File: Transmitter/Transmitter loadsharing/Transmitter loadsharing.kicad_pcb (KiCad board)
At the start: 4 copper layers, 145 x 50.8 mm, 115 parts, among them J1 Conn_Coaxial, J10 Conn_01x01, J11 Conn_01x01, J12 Conn_01x01, J13 Conn_01x01, J14 Conn_01x01, J15 Conn_01x01, J16 Conn_01x01, J17 Conn_Coaxial, J18 Conn_Coaxial, J19 Conn_Coaxial, J2 Conn_01x03, J20 Conn_01x01, J21 Conn_01x01, J22 Conn_01x01, J23 Conn_01x01, J24 Conn_01x01, J25 Conn_01x01, J3 Conn_01x03, J4 Conn_01x02_Socket, J5 Conn_01x02, J6 Conn_01x01, J7 Conn_01x02, J8 Conn_01x02_Socket, J9 Conn_01x01, U1 OPA3692IDBQR, U10 LT3094EMSE-PBF, U11 LT3094EMSE-PBF, U2 THS3091D, U3 THS3091D, U4 THS3091D, U5 THS3091D, U6 THS3091D, U7 THS3091D, U8 LT3045EMSE-PBF, U9 LT3045EMSE-PBF

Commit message: version before review with Saul
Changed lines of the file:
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@@
 			)
 		)
-		(property ki_fp_filters "*BNC* *SMA* *SMB* *SMC* *Cinch* *LEMO* *UMRF* *MCX* *U.FL*")
-		(sheetname "Root")
-		(sheetfile "Transmitter loadsharing.kicad_sch")
 		(attr through_hole)
 		(fp_line
@@
 		)
 		(model "${KICAD8_3DMODEL_DIR}/Connector_Coaxial.3dshapes/BNC_Amphenol_B6252HB-NPP3G-50_Horizontal.wrl"
+			(hide yes)
 			(offset
 				(xyz 0 0 0)
@@
 			)
 		)
+		(model "C:/Projects/KiCad/Spiral/Kicad Degree project GIT/Degree-Project-KiCad/B6252HB-NPP3G-50/3D/B6252HB-NPP3G-50.stp"
+			(offset
+				(xyz 0 -1 8)
+			)
+			(scale
+				(xyz 1 1 1)
+			)
+			(rotate
+				(xyz -90 0 180)
+			)
+		)
 	)
 	(footprint "Opa3692 SOIC:DBQ16"
@@
 			)
 		)
-		(property ki_fp_filters "*BNC* *SMA* *SMB* *SMC* *Cinch* *LEMO* *UMRF* *MCX* *U.FL*")
-		(sheetname "Root")
-		(sheetfile "Transmitter loadsharing.kicad_sch")
 		(attr through_hole)
 		(fp_line
@@
 		)
 		(model "${KICAD8_3DMODEL_DIR}/Connector_Coaxial.3dshapes/BNC_Amphenol_B6252HB-NPP3G-50_Horizontal.wrl"
+			(hide yes)
 			(offset
 				(xyz 0 0 0)
@@
 			)
 		)
+		(model "C:/Projects/KiCad/Spiral/Kicad Degree project GIT/Degree-Project-KiCad/B6252HB-NPP3G-50/3D/B6252HB-NPP3G-50.stp"
+			(offset
+				(xyz 0 -1 8)
+			)
+			(scale
+				(xyz 1 1 1)
+			)
+			(rotate
+				(xyz -90 0 180)
+			)
+		)
 	)
 	(footprint "Capacitor_SMD:C_0603_1608Metric_Pad1.08x0.95mm_HandSolder"
@@
 		(tags "resistor handsolder")
 		(property "Reference" "R26"
-			(at 0 -1.43 90)
-			(layer "B.SilkS")
+			(at 0 -1.43 -90)
+			(layer "F.SilkS")
 			(effects
 				(font
@@
 					(thickness 0.15)
 				)
-				(justify mirror)
 			)
 		)

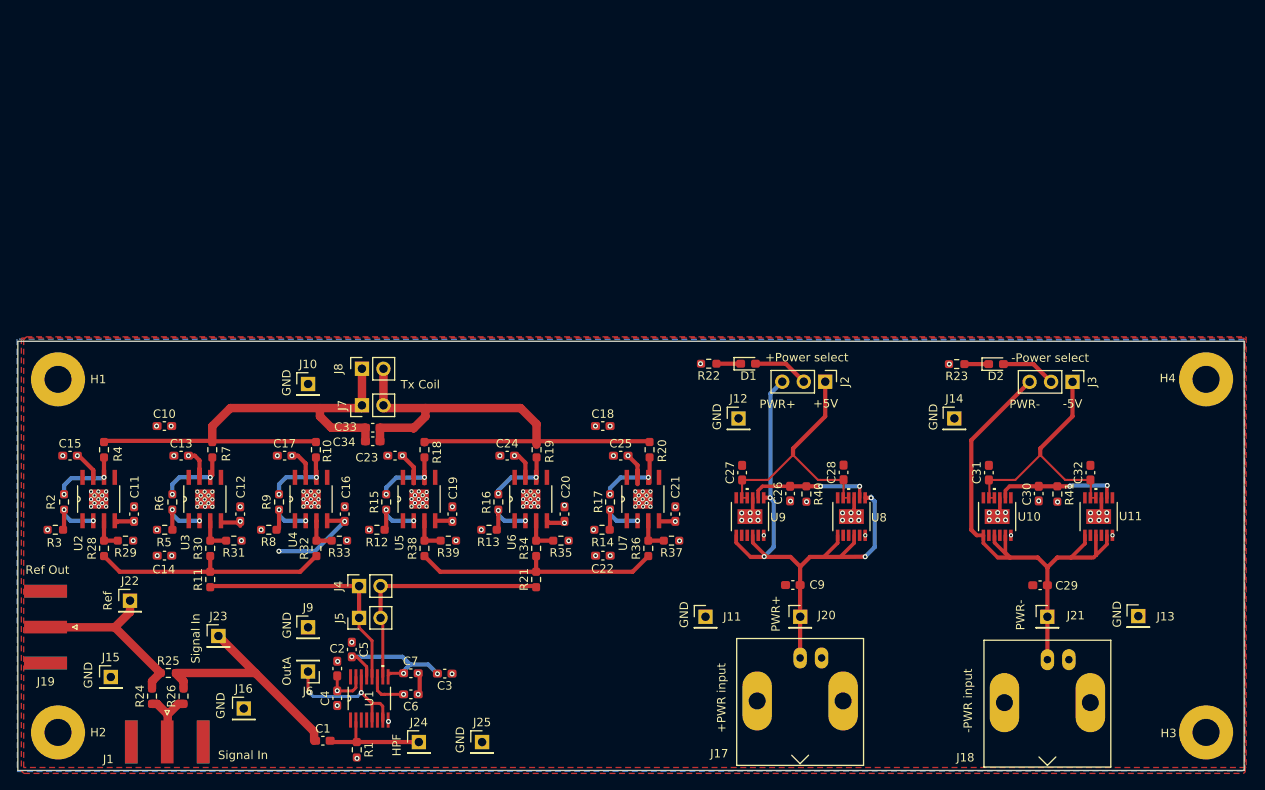
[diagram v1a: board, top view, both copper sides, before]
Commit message: Added via stiching to TX board, moved almost all vias off of pads, increased the trace width for the power supply and changed coil connector to horizontal socket
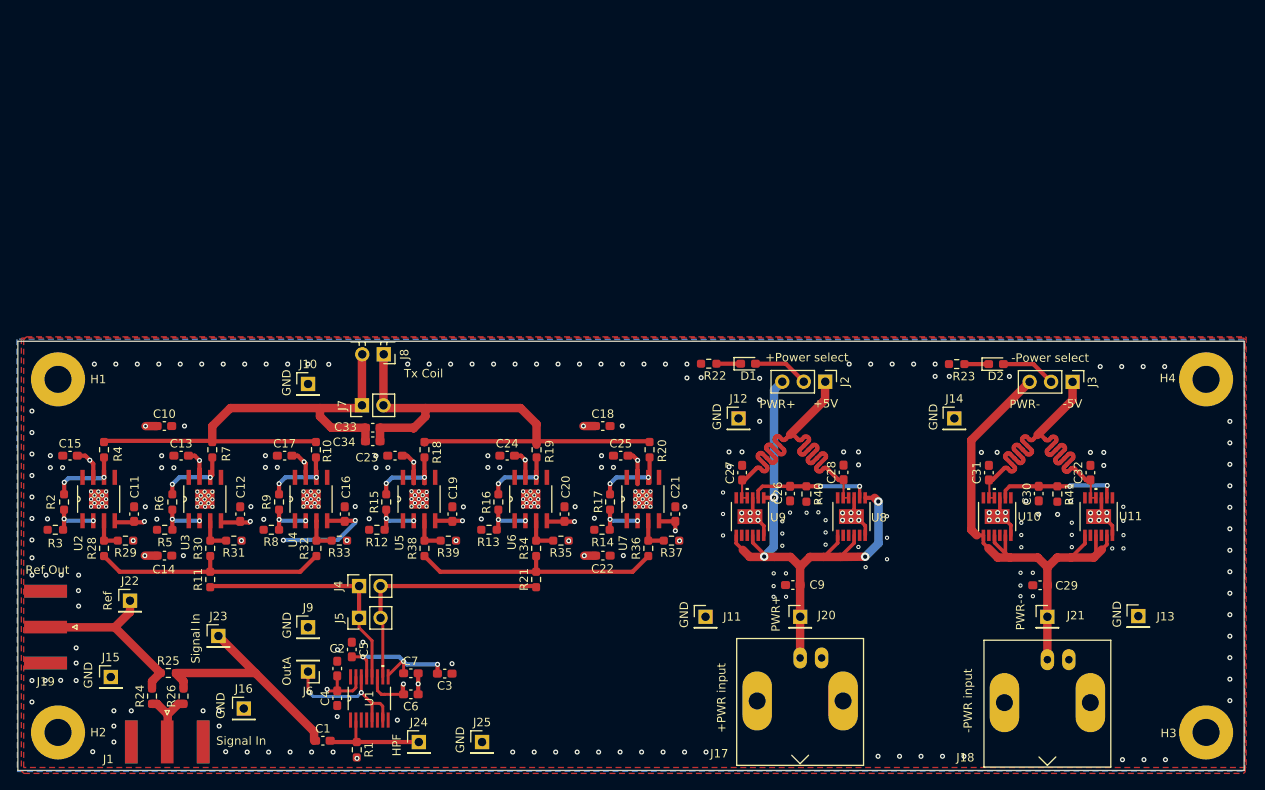
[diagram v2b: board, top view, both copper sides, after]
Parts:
- C11, C12, C13, C15, C16, C17, C19, C20, C21, C23, C24, C25: value 0.1 nF -> 0.1 uF
- J8: footprint Connector_PinSocket_2.54mm:PinSocket_1x02_P2.54mm_Vertical -> Connector_PinSocket_2.54mm:PinSocket_1x02_P2.54mm_Horizontal
- moved J8 3.09 mm to (129.8, 89.4), turned to -90 degrees
- moved R8 0.30 mm to (116.5, 110.1)
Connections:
- J8 pad 1: /coil load start -> /coil load end
- J8 pad 2: /coil load end -> /coil load start
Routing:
- net /-5V_In: track 30.2 -> 50.0 mm
- net /+5V_In: track 30.2 -> 50.0 mm
- net -5V: track 48.0 -> 57.1 mm
- net GND: track 10.1 -> 18.5 mm, vias 148 -> 313
- net +5V: track 42.7 -> 50.8 mm
- net /coil load end: track 61.9 -> 63.7 mm
- net /coil load start: track 58.6 -> 60.1 mm
- net Net-(U4-VIN-): track 6.53 -> 5.64 mm
- net Net-(U2-VIN-): track 6.79 -> 5.91 mm
- net Net-(U3-VIN-): track 6.10 -> 5.31 mm
- net /PWR+: track 69.3 -> 70.0 mm
- net Net-(U6-VIN-): track 6.33 -> 5.70 mm
- net Net-(U6-VOUT): track 8.49 -> 9.05 mm

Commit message: Fixed spacing between ICs, tried to make traces the same length each of the loadsharing op-amps
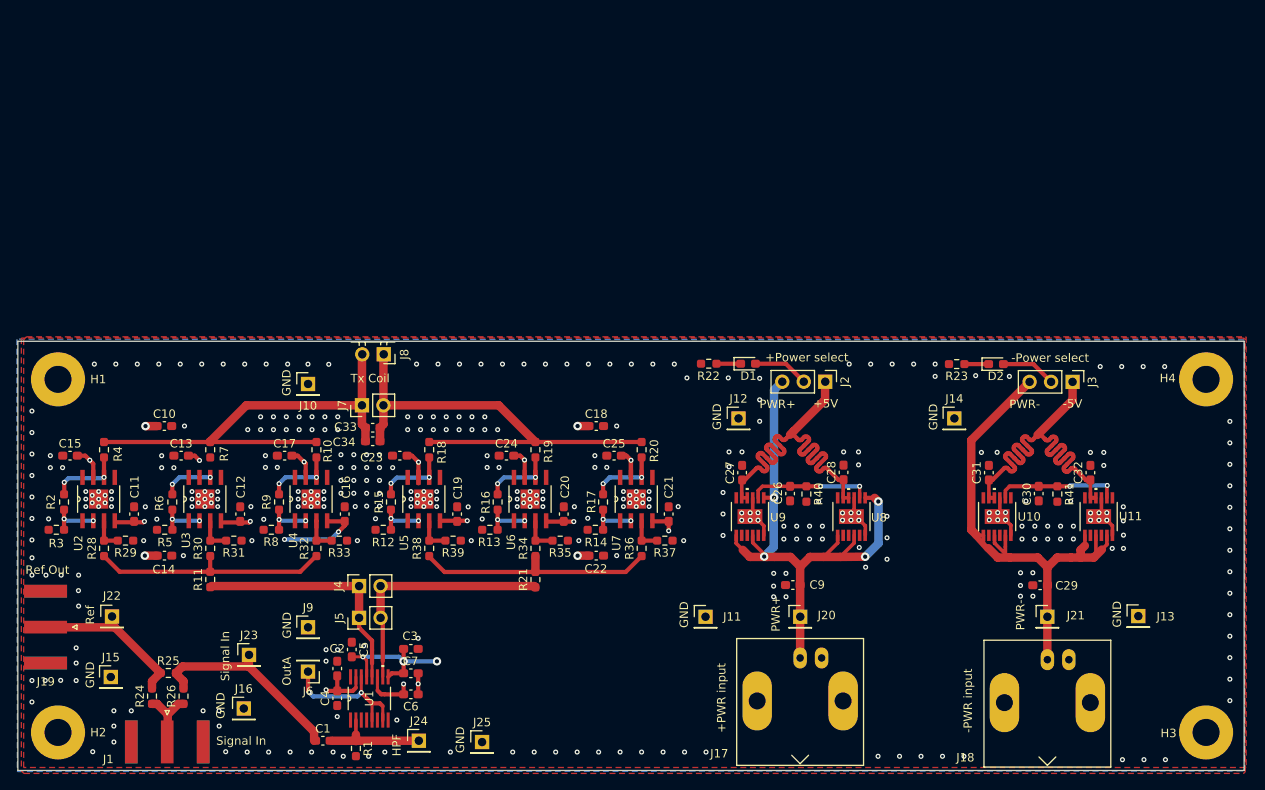
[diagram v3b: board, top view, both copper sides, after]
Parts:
- moved C3 4.96 mm to (133.0, 124.2)
- moved J23 4.25 mm to (113.8, 124.9)
- moved J22 2.83 mm to (97.6, 120.4)
- moved R20 0.94 mm to (160.2, 100.6)
- moved R17 0.82 mm to (155.7, 106.8)
- moved C21 0.79 mm to (163.4, 108.3)
- moved C22 0.79 mm to (154.9, 113.2)
- moved C25 0.79 mm to (157.0, 101.4)
- moved R14 0.79 mm to (154.8, 110.1)
- moved R36 0.79 mm to (160.2, 112.3)
- moved R37 0.79 mm to (163.0, 111.4)
- moved U7 0.79 mm to (159.6, 106.5)
- moved C18 0.77 mm to (154.9, 97.8)
- moved R12 0.75 mm to (129.7, 110.1)
- moved C19 0.56 mm to (138.4, 108.3)
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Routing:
- net /coil load end: track 63.7 -> 55.6 mm
- net +5V: track 50.8 -> 44.8 mm
- net /coil load start: track 60.1 -> 55.4 mm
- net Net-(J23-Pin_1): track 28.7 -> 24.5 mm
- net -5V: track 57.1 -> 54.1 mm
- net /Ref out: track 21.8 -> 19.4 mm
- net Net-(U3-VOUT): track 8.40 -> 6.02 mm
- net /PWR-: track 63.1 -> 64.9 mm
- net /loadshare input -: track 29.9 -> 28.6 mm
- net GND: vias 313 -> 364

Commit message: git being weird
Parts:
- C10, C14, C18, C2, C22, C3: value 6.8 uF -> 6.8uF
- C11, C12, C13, C15, C16, C17, C19, C20, C21, C23, C24, C25, C4: value 0.1 uF -> 0.1uF
- C26, C30: value 0.47u -> 0.47uF
- C27, C28, C31, C32, C9: value 10u -> 10uF
- C29: value 22u -> 22uF
- R1, R24, R25, R26: value 50 Ohm -> 50Ω
- R10, R18, R19, R20, R4, R7: value R -> Ro
- R11, R21: value 1 Ohm -> 1Ω
- R12, R13, R14, R3, R5, R8: value 250 Ohm -> Rg
- R15, R16, R17, R2, R6, R9: value 1 kOhm -> Rf
- R22, R23: value R -> Rled
- R29, R31, R33, R35, R37, R39: value R -> Rt
- R30, R32, R34, R36, R38: value 0 Ohm -> 0Ω
- moved R41 37.8 mm to (209.6, 68.1)
- moved C1 37.8 mm to (122.8, 97.2)
- moved C11 37.8 mm to (100.5, 70.4)
- moved C12 37.8 mm to (113.0, 70.4)
- moved C16 37.8 mm to (125.4, 70.4)
- moved C19 37.8 mm to (138.7, 70.4)
- moved C2 37.8 mm to (124.5, 88.7)
- moved C20 37.8 mm to (151.3, 70.4)
- moved C21 37.8 mm to (163.7, 70.4)
- moved C26 37.8 mm to (178.1, 68.0)
- moved C30 37.8 mm to (207.5, 68.0)
- moved C5 37.8 mm to (126.2, 86.4)
- moved C7 37.8 mm to (133.2, 89.3)
- moved C9 37.8 mm to (178.4, 78.8)
- moved H2 37.8 mm to (91.5, 96.2)
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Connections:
- U10 pad 12: unconnected-(U10-OUT-Pad12) -> /-5V_In
- U10 pad 13: GND -> /PWR-
- U10 pad 2: unconnected-(U10-IN-Pad2) -> /PWR-
- U11 pad 12: unconnected-(U11-OUT-Pad12) -> /-5V_In
- U11 pad 13: GND -> /PWR-
- U11 pad 2: unconnected-(U11-IN-Pad2) -> /PWR-
- U8 pad 12: unconnected-(U8-OUT-Pad12) -> /+5V_In
- U8 pad 2: unconnected-(U8-IN-Pad2) -> /PWR+
- U8 pad 3: unconnected-(U8-IN-Pad3) -> /PWR+
- U9 pad 12: unconnected-(U9-OUT-Pad12) -> /+5V_In
- U9 pad 2: unconnected-(U9-IN-Pad2) -> /PWR+
- U9 pad 3: unconnected-(U9-IN-Pad3) -> /PWR+
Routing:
- net /+5V_In: track 50.0 -> 57.8 mm
- net /PWR+: track 70.0 -> 63.6 mm
- net /-5V_In: track 49.7 -> 55.7 mm
- net Net-(U3-VOUT): track 6.02 -> 8.37 mm
- net +5V: track 44.8 -> 46.8 mm
- net GND: track 18.5 -> 16.6 mm, vias 364 -> 299
- net /PWR-: track 64.9 -> 64.3 mm
- added copper zone on F.Cu, net /PWR+
- added copper zone on F.Cu, net /PWR-

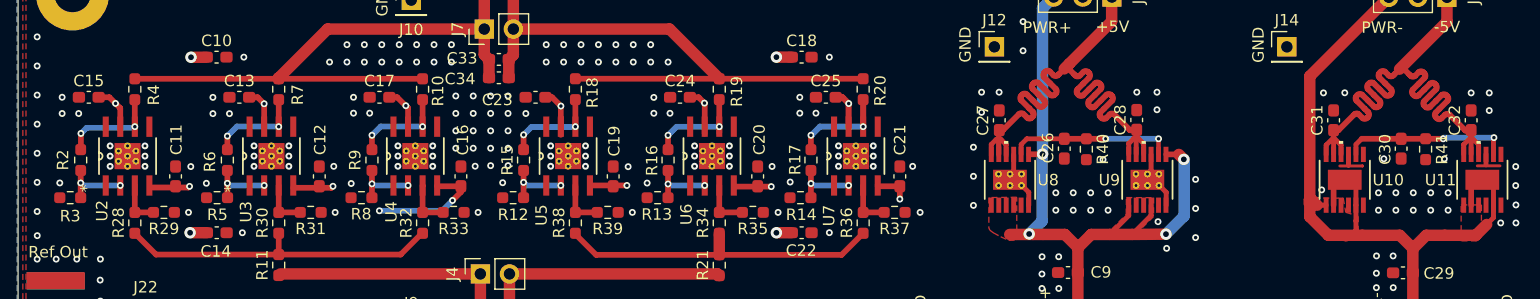
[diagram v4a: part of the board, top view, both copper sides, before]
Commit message: Changed symbol for THS to add EPAD connection, fixed thermal vias on footprint, fixed THS3091 dir
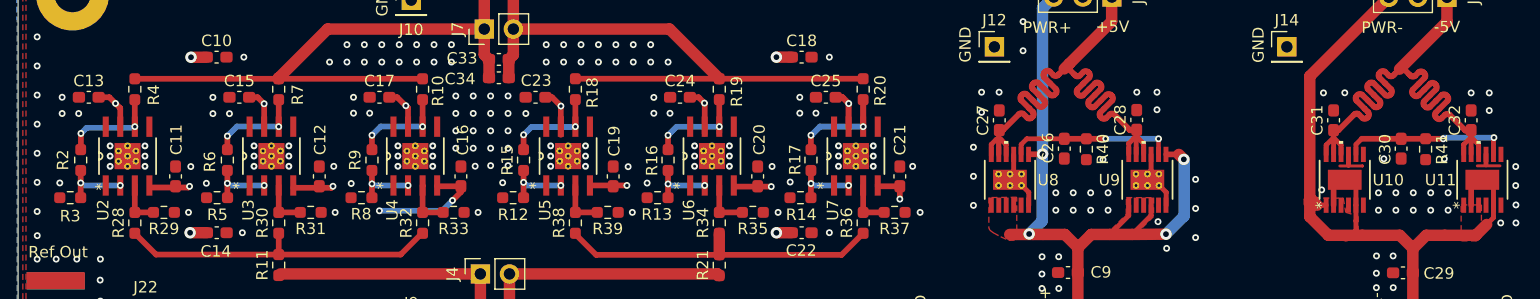
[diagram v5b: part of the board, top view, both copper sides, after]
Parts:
- U3, U4, U5, U6, U7: footprint THS3091DDR:DDA8_2P28X2P28 -> THS3091:DDA8_2P28X2P28
- renumbered C15 to C13, C13 to C15
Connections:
- C27 pad 1: /+5V_In -> +5V
- C28 pad 1: /+5V_In -> +5V
- C31 pad 1: /-5V_In -> -5V
- C32 pad 1: /-5V_In -> -5V
- J2 pad 1: /+5V_In -> +5V
- J3 pad 1: /-5V_In -> -5V
- U10 pad 10: /-5V_In -> -5V
- U10 pad 11: /-5V_In -> -5V
- U10 pad 12: /-5V_In -> -5V
- U11 pad 10: /-5V_In -> -5V
- U11 pad 11: /-5V_In -> -5V
- U11 pad 12: /-5V_In -> -5V
- U8 pad 10: /+5V_In -> +5V
- U8 pad 11: /+5V_In -> +5V
- U8 pad 12: /+5V_In -> +5V
- U9 pad 10: /+5V_In -> +5V
- U9 pad 11: /+5V_In -> +5V
- U9 pad 12: /+5V_In -> +5V
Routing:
- net +5V: track 46.8 -> 104.6 mm
- net /+5V_In: track 57.8 -> 0.00 mm
- net -5V: track 54.1 -> 109.8 mm
- net /-5V_In: track 55.7 -> 0.00 mm

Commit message: Drew a footprint for a BNC edge connector 112640, made sure coils are centered and as symmetrical as possible:wq
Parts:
- J8: value Conn_01x02_Socket -> Conn_01x02_Socket Horizontal
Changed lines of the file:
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@@
 			)
 		)
-		(property "Footprint" "DDA8_2P28X2P28"
+		(property "Footprint" "THS3091:DDA8_2P28X2P28"
 			(at 0 0 90)
 			(unlocked yes)
@@
 			)
 		)
-		(property "Footprint" "DDA8_2P28X2P28"
+		(property "Footprint" "THS3091:DDA8_2P28X2P28"
 			(at 0 0 90)
 			(unlocked yes)
@@
 			)
 		)
-		(property "Footprint" "DDA8_2P28X2P28"
+		(property "Footprint" "THS3091:DDA8_2P28X2P28"
 			(at 0 0 90)
 			(unlocked yes)
@@
 			)
 		)
-		(property "Footprint" "DDA8_2P28X2P28"
+		(property "Footprint" "THS3091:DDA8_2P28X2P28"
 			(at 0 0 90)
 			(unlocked yes)
@@
 			)
 		)
-		(property "Value" "Conn_01x02_Socket"
-			(at -3.5126 -9.7062 180)
+		(property "Value" "Conn_01x02_Socket Horizontal"
+			(at -3.1526 -14.0762 180)
 			(layer "F.Fab")
 			(effects
@@
 			)
 		)
-		(property "Footprint" "DDA8_2P28X2P28"
+		(property "Footprint" "THS3091:DDA8_2P28X2P28"
 			(at 0 0 90)
 			(unlocked yes)

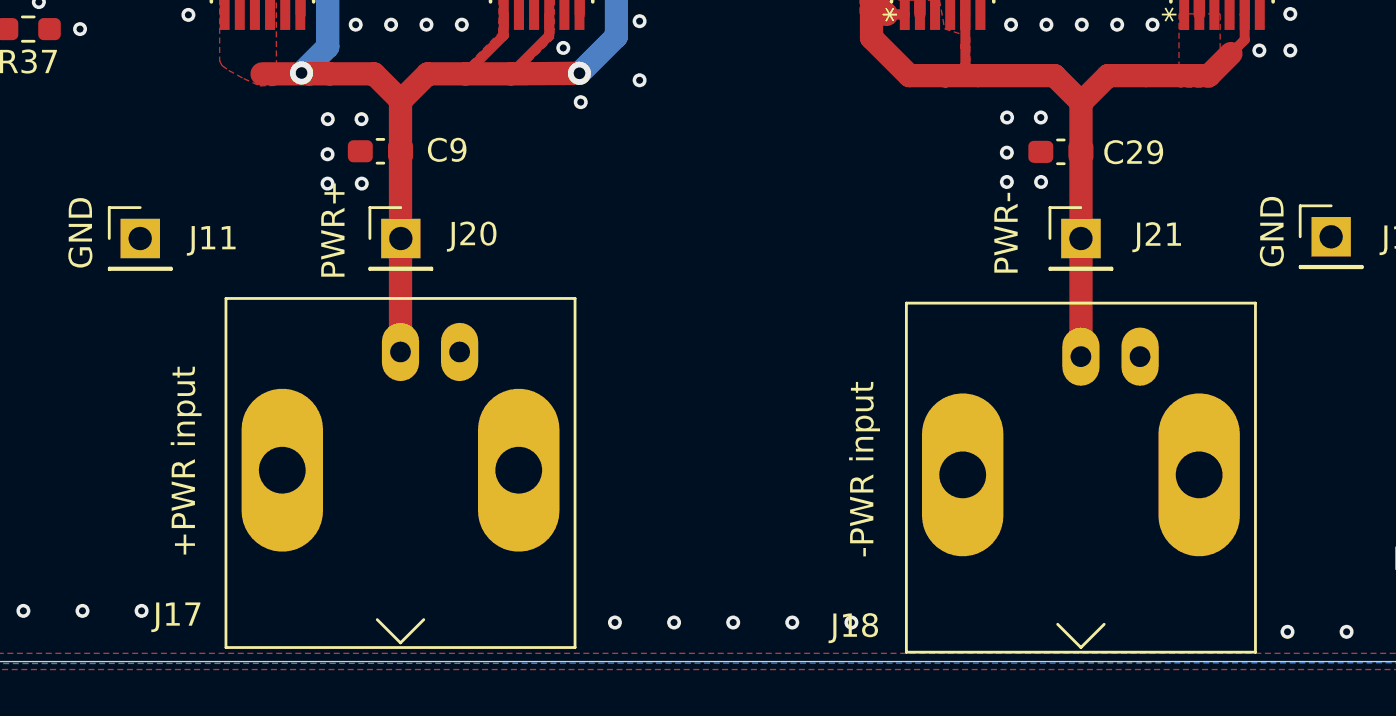
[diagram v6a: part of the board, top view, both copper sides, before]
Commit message: added LTM8049 symbol/footprint
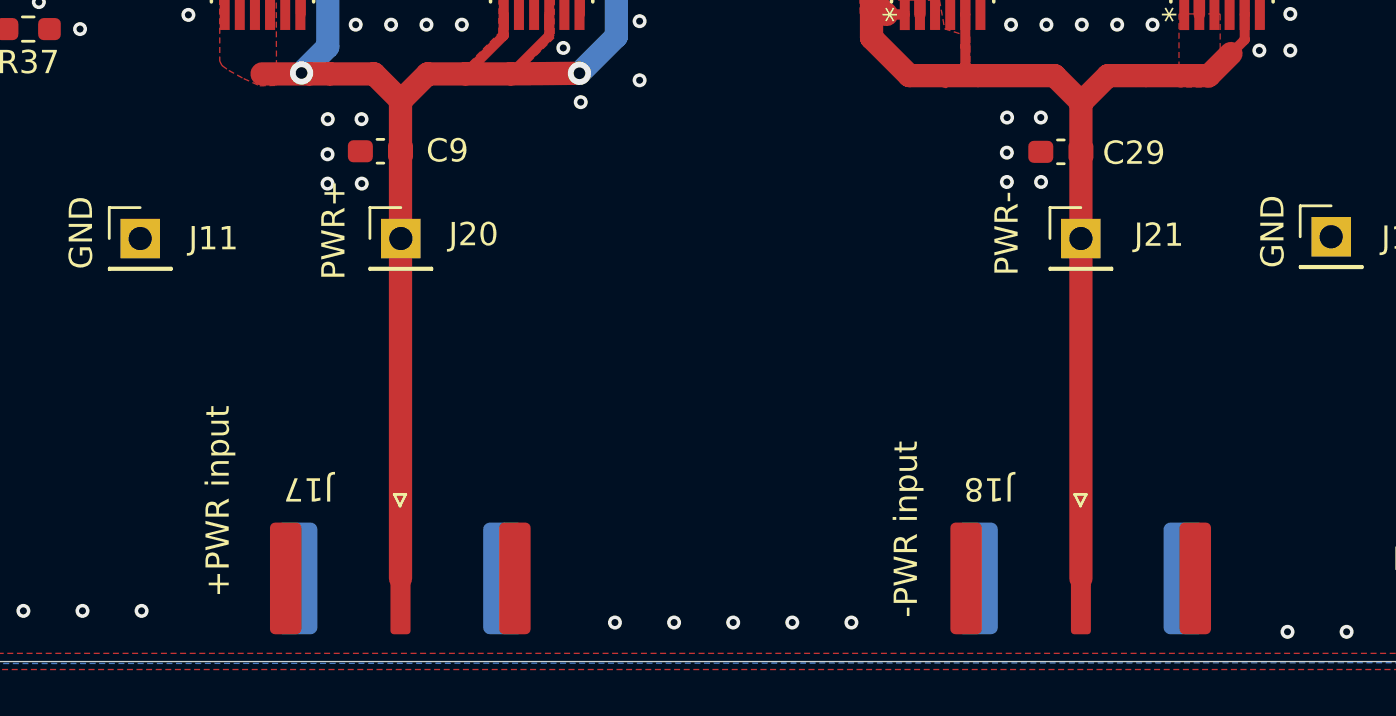
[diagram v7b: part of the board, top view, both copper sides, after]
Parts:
- J17, J18: footprint Connector_Coaxial:BNC_Amphenol_B6252HB-NPP3G-50_Horizontal -> BNc_Amphenol_112640:BNC_Amphenol_112640_Edge_mount
- R28: value 0 Ohm -> 0Ω
- moved J17 7.36 mm to (179.2, 94.8), turned to -90 degrees
- moved J18 7.16 mm to (208.5, 94.8), turned to -90 degrees
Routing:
- net /PWR+: track 63.6 -> 73.3 mm
- net /PWR-: track 64.3 -> 73.8 mm
